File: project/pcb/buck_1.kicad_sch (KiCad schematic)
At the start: 12 parts, among them J1 12V FUSED INPUT, J2 LOAD + / -, Q1 IRFZ44N TO-220

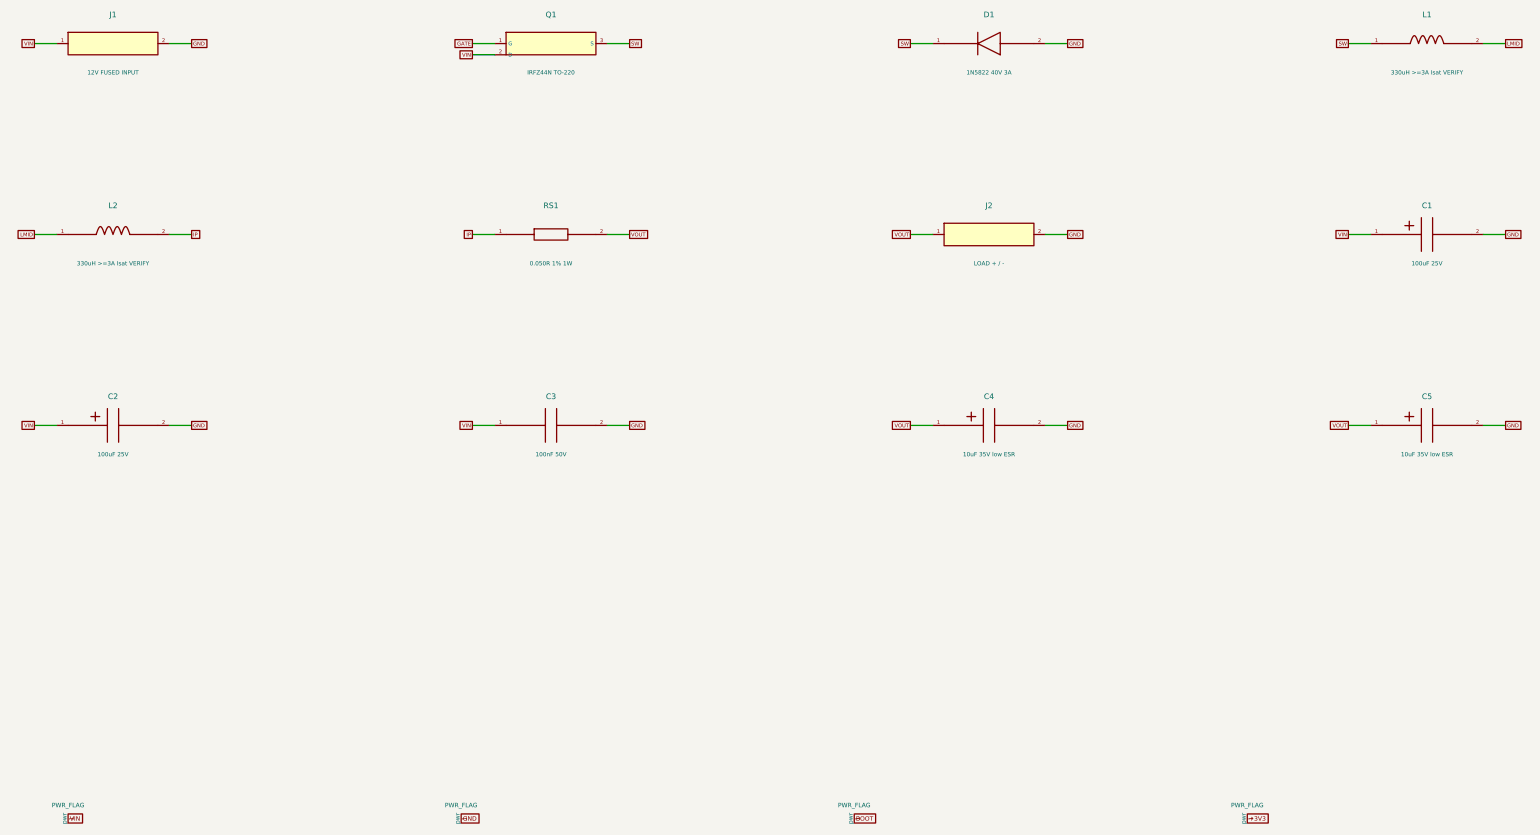
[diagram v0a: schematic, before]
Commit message: Preserve Buck PCB design and add validated JLCPCB quote package
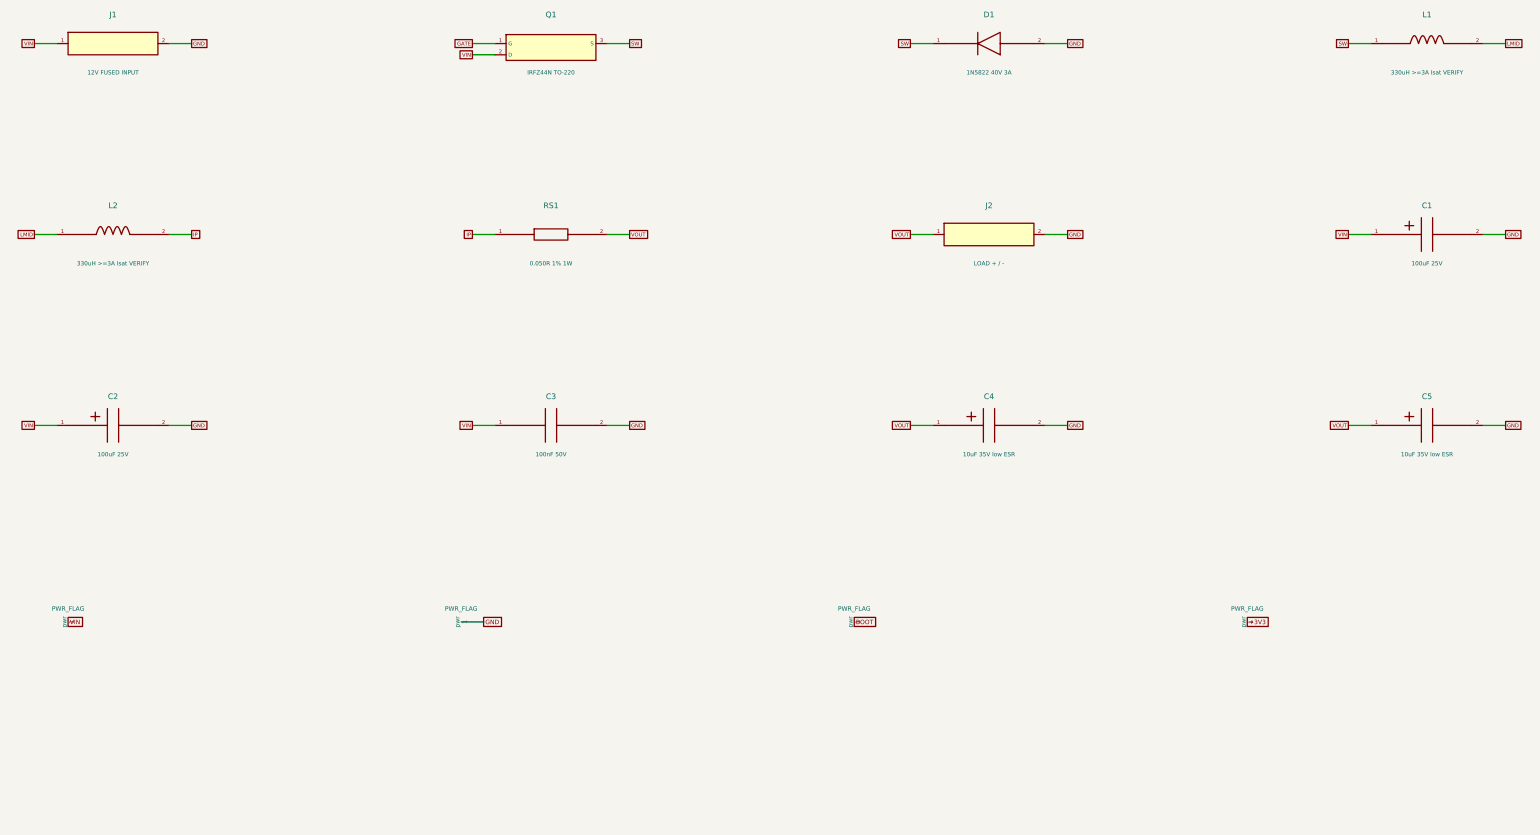
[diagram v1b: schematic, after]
